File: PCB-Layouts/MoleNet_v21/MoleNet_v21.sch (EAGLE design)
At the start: 31 parts, among them IC1 25LC080P, Q1 BS250, Q2 BS170, U1 MCP1703-5002E/DB, U2 ATMEGA328P-PU, U3 RFM69CW, X1 SMA-142-0711-821/826

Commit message: MoleNet version 2.1 ready
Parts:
- added JP7: (no value), pinhead:PINHD-1X6
- added JP8: (no value), pinhead:PINHD-1X3
- JP3: value ISP -> (none); device pinhead:PINHD-2X5 -> pinhead:PINHD-1X3
- JP4: device pinhead:PINHD-1X4 -> pinhead:PINHD-1X3
- JP6: value (none) -> ISP; device pinhead:PINHD-1X6 -> pinhead:PINHD-2X5
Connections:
- new net N$2: JP3.2, Q1.S, R2.2
- new net SENSRXD: C11.1, JP8.3, K1.3
- net +12V: now also JP3.1; no longer Q1.S, R2.2
- net D4: now also JP4.3; no longer JP4.4
- net D5: now also JP4.2; no longer JP4.3
- net D6: now also JP4.1; no longer JP4.2
- net D8: now also JP8.1; no longer JP4.1
- net GND: now also JP6.10, JP6.4, JP6.8, JP7.5, JP7.6; no longer JP3.10, JP3.4, JP3.6, JP3.8, JP6.5
- net MISO: now also JP6.9; no longer JP3.9
- net MOSI: now also JP6.1; no longer JP3.1
- net N$9: now also JP7.1; no longer JP6.1
- net RESET: now also JP6.5; no longer JP3.5
- net RXD: now also JP7.3, JP8.2; no longer C11.1, JP6.3, K1.3
- net SCK: now also JP6.7; no longer JP3.7
- net TXD: now also JP7.2; no longer JP6.2
- net VCC: now also JP3.3, JP6.2, JP7.4; no longer JP3.2, JP6.4
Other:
- moved on the sheet: C11, C12, K1, Q1, Q2, R2, RTC-1, RTC-2, RTC-3, RTC-4, RTC-5, RTC-6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

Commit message: MoleNet version 2.1 rtm
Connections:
- net RXD: now also JP8.3; no longer JP8.2
- net SENSRXD: now also JP8.2; no longer JP8.3
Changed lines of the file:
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@@
-</segment>
-<segment>
-<wire x1="210.82" y1="38.1" x2="195.58" y2="38.1" width="0.1524" layer="91"/>
-<label x="195.58" y="38.1" size="1.778" layer="95"/>
-<pinref part="JP8" gate="A" pin="2"/>
 </segment>
 <segment>
@@
 <wire x1="50.8" y1="40.64" x2="35.56" y2="40.64" width="0.1524" layer="91"/>
 <label x="35.56" y="40.64" size="1.778" layer="95"/>
+</segment>
+<segment>
+<wire x1="210.82" y1="35.56" x2="195.58" y2="35.56" width="0.1524" layer="91"/>
+<label x="195.58" y="35.56" size="1.778" layer="95"/>
+<pinref part="JP8" gate="A" pin="3"/>
 </segment>
 </net>
@@
 <net name="SENSRXD" class="0">
 <segment>
-<wire x1="210.82" y1="35.56" x2="195.58" y2="35.56" width="0.1524" layer="91"/>
-<label x="195.58" y="35.56" size="1.778" layer="95"/>
-<pinref part="JP8" gate="A" pin="3"/>
-</segment>
-<segment>
 <pinref part="K1" gate="G$1" pin="3"/>
 <label x="154.94" y="30.48" size="1.778" layer="95"/>
 <pinref part="C11" gate="G$1" pin="1"/>
 <wire x1="165.1" y1="30.48" x2="152.4" y2="30.48" width="0.1524" layer="91"/>
+</segment>
+<segment>
+<wire x1="210.82" y1="38.1" x2="195.58" y2="38.1" width="0.1524" layer="91"/>
+<label x="195.58" y="38.1" size="1.778" layer="95"/>
+<pinref part="JP8" gate="A" pin="2"/>
 </segment>
 </net>
@@
 </sheet>
 </sheets>
-<errors>
-</errors>
 </schematic>
 </drawing>

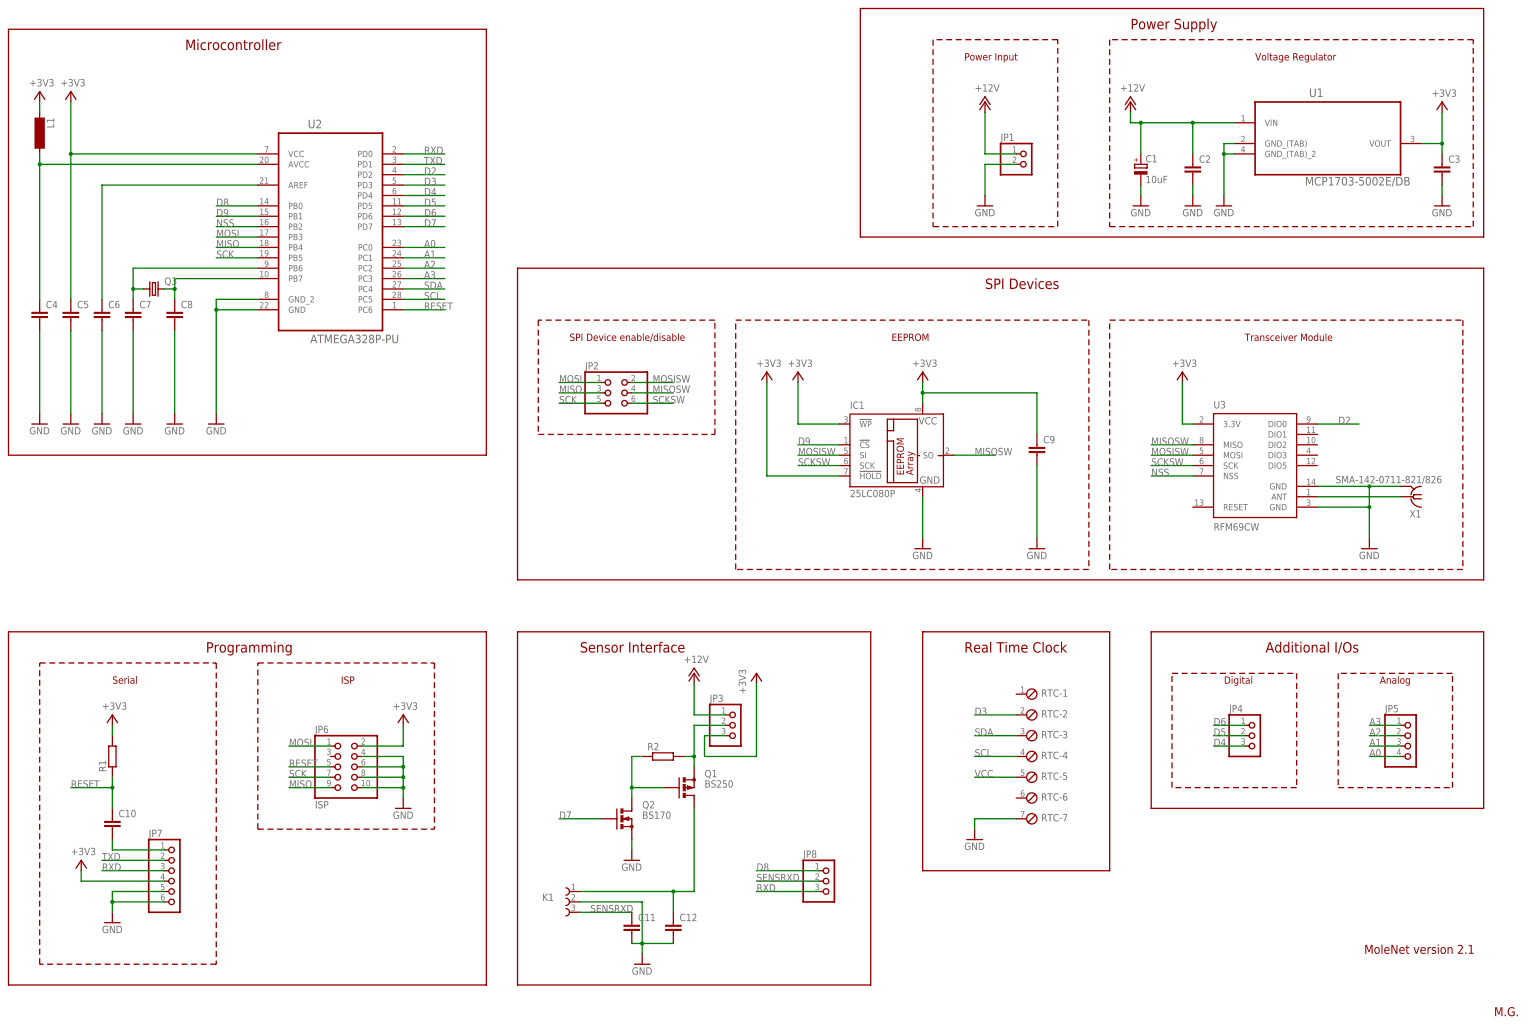
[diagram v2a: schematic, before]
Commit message: added/corrected part values in all layouts; created partlist for version 2.1
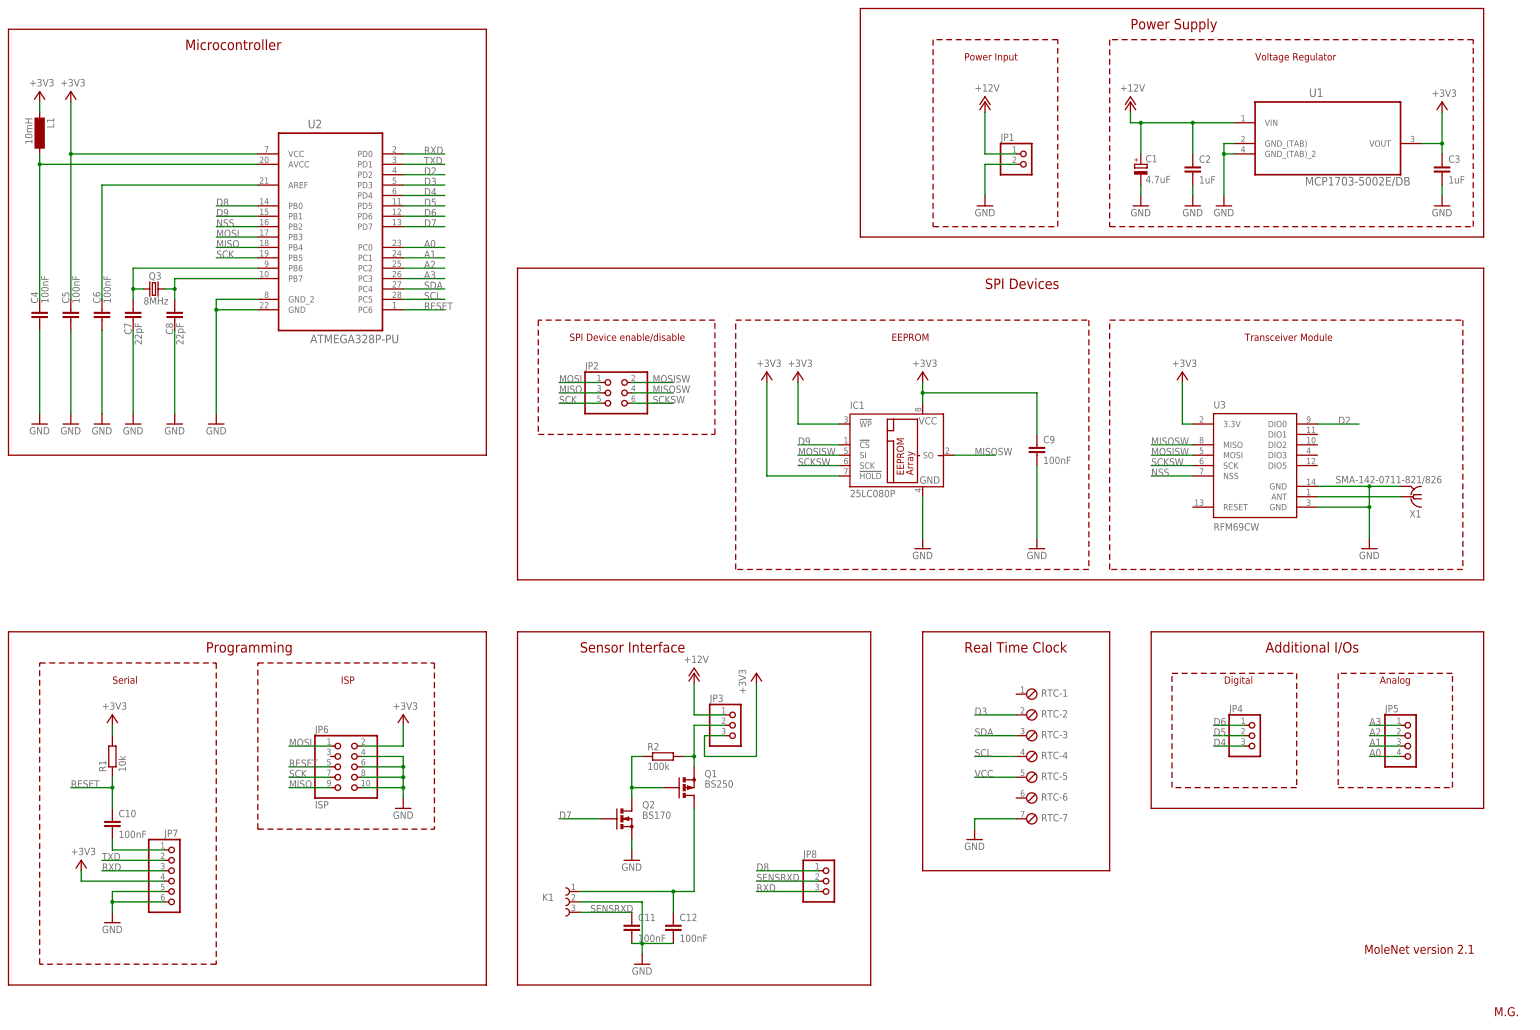
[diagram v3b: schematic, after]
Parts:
- C1: value 10uF -> 4.7uF
- C10, C11, C12, C4, C5, C6, C9: value (none) -> 100nF
- C2, C3: value (none) -> 1uF
- C7, C8: value (none) -> 22pF
- L1: value (none) -> 10mH
- Q3: value (none) -> 8MHz
- R1: value (none) -> 10k
- R2: value (none) -> 100k
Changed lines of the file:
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@@
 <setting verticaltext="up"/>
 </settings>
-<grid distance="0.1" unitdist="inch" unit="inch" style="lines" multiple="1" display="yes" altdistance="0.01" altunitdist="inch" altunit="inch"/>
+<grid distance="100" unitdist="mil" unit="mil" style="lines" multiple="1" display="no" altdistance="0.01" altunitdist="inch" altunit="inch"/>
 <layers>
 <layer number="1" name="Top" color="4" fill="1" visible="no" active="no"/>
@@
 <part name="Q1" library="transistor-small-signal" deviceset="BS250" device=""/>
 <part name="GND1" library="supply1" deviceset="GND" device=""/>
-<part name="R2" library="resistor" deviceset="R-EU_" device="0207/10"/>
+<part name="R2" library="resistor" deviceset="R-EU_" device="0207/10" value="100k"/>
 <part name="+3V1" library="supply1" deviceset="+3V3" device=""/>
 <part name="GND2" library="supply1" deviceset="GND" device=""/>
-<part name="L1" library="inductor-neosid" deviceset="BS" device="11"/>
-<part name="C1" library="resistor" deviceset="CPOL-EU" device="E2.5-6" value="10uF"/>
-<part name="C2" library="resistor" deviceset="C-EU" device="025-025X050"/>
-<part name="C3" library="resistor" deviceset="C-EU" device="025-025X050"/>
-<part name="C4" library="resistor" deviceset="C-EU" device="025-025X050"/>
+<part name="L1" library="inductor-neosid" deviceset="BS" device="11" value="10mH"/>
+<part name="C1" library="resistor" deviceset="CPOL-EU" device="E2.5-6" value="4.7uF"/>
+<part name="C2" library="resistor" deviceset="C-EU" device="025-025X050" value="1uF"/>
+<part name="C3" library="resistor" deviceset="C-EU" device="025-025X050" value="1uF"/>
+<part name="C4" library="resistor" deviceset="C-EU" device="025-025X050" value="100nF"/>
 <part name="GND3" library="supply1" deviceset="GND" device=""/>
-<part name="C6" library="resistor" deviceset="C-EU" device="025-025X050"/>
+<part name="C6" library="resistor" deviceset="C-EU" device="025-025X050" value="100nF"/>
 <part name="GND4" library="supply1" deviceset="GND" device=""/>
 <part name="+3V2" library="supply1" deviceset="+3V3" device=""/>
@@
 <part name="GND12" library="supply1" deviceset="GND" device=""/>
 <part name="FRAME1" library="frames" deviceset="A3L-LOC" device=""/>
-<part name="C5" library="resistor" deviceset="C-EU" device="025-025X050"/>
+<part name="C5" library="resistor" deviceset="C-EU" device="025-025X050" value="100nF"/>
 <part name="GND13" library="supply1" deviceset="GND" device=""/>
 <part name="JP7" library="pinhead" deviceset="PINHD-1X6" device=""/>
 <part name="GND14" library="supply1" deviceset="GND" device=""/>
 <part name="+3V8" library="supply1" deviceset="+3V3" device=""/>
-<part name="C10" library="resistor" deviceset="C-EU" device="025-025X050"/>
-<part name="R1" library="resistor" deviceset="R-EU_" device="0207/10"/>
+<part name="C10" library="resistor" deviceset="C-EU" device="025-025X050" value="100nF"/>
+<part name="R1" library="resistor" deviceset="R-EU_" device="0207/10" value="10k"/>
 <part name="+3V9" library="supply1" deviceset="+3V3" device=""/>
-<part name="Q3" library="crystal" deviceset="CRYSTAL" device="HC18U-V"/>
-<part name="C7" library="resistor" deviceset="C-EU" device="025-025X050"/>
-<part name="C8" library="resistor" deviceset="C-EU" device="025-025X050"/>
+<part name="Q3" library="crystal" deviceset="CRYSTAL" device="HC18U-V" value="8MHz"/>
+<part name="C7" library="resistor" deviceset="C-EU" device="025-025X050" value="22pF"/>
+<part name="C8" library="resistor" deviceset="C-EU" device="025-025X050" value="22pF"/>
 <part name="GND16" library="supply1" deviceset="GND" device=""/>
 <part name="GND17" library="supply1" deviceset="GND" device=""/>
@@
 <part name="GND18" library="supply1" deviceset="GND" device=""/>
 <part name="+3V10" library="supply1" deviceset="+3V3" device=""/>
-<part name="C9" library="resistor" deviceset="C-EU" device="025-025X050"/>
+<part name="C9" library="resistor" deviceset="C-EU" device="025-025X050" value="100nF"/>
 <part name="GND19" library="supply1" deviceset="GND" device=""/>
-<part name="C11" library="resistor" deviceset="C-EU" device="025-025X050"/>
-<part name="C12" library="resistor" deviceset="C-EU" device="025-025X050"/>
+<part name="C11" library="resistor" deviceset="C-EU" device="025-025X050" value="100nF"/>
+<part name="C12" library="resistor" deviceset="C-EU" device="025-025X050" value="100nF"/>
 <part name="JP2" library="pinhead" deviceset="PINHD-2X3" device=""/>
 <part name="JP5" library="pinhead" deviceset="PINHD-1X4" device=""/>
@@
 <instance part="C2" gate="G$1" x="302.26" y="213.36"/>
 <instance part="C3" gate="G$1" x="363.22" y="213.36"/>
-<instance part="C4" gate="G$1" x="20.32" y="177.8"/>
+<instance part="C4" gate="G$1" x="20.32" y="177.8" smashed="yes">
+<attribute name="NAME" x="19.939" y="179.324" size="1.778" layer="95" rot="R90"/>
+<attribute name="VALUE" x="22.479" y="179.324" size="1.778" layer="96" rot="R90"/>
+</instance>
 <instance part="GND3" gate="1" x="20.32" y="149.86"/>
-<instance part="C6" gate="G$1" x="35.56" y="177.8"/>
+<instance part="C6" gate="G$1" x="35.56" y="177.8" smashed="yes">
+<attribute name="NAME" x="35.179" y="179.324" size="1.778" layer="95" rot="R90"/>
+<attribute name="VALUE" x="37.719" y="179.324" size="1.778" layer="96" rot="R90"/>
+</instance>
 <instance part="GND4" gate="1" x="35.56" y="149.86"/>
 <instance part="+3V2" gate="G$1" x="27.94" y="231.14" smashed="yes">
@@
 <instance part="GND12" gate="1" x="309.88" y="203.2"/>
 <instance part="FRAME1" gate="G$1" x="0" y="0"/>
-<instance part="C5" gate="G$1" x="27.94" y="177.8"/>
+<instance part="C5" gate="G$1" x="27.94" y="177.8" smashed="yes">
+<attribute name="NAME" x="27.559" y="179.324" size="1.778" layer="95" rot="R90"/>
+<attribute name="VALUE" x="30.099" y="179.324" size="1.778" layer="96" rot="R90"/>
+</instance>
 <instance part="GND13" gate="1" x="27.94" y="149.86"/>
-<instance part="JP7" gate="A" x="53.34" y="38.1"/>
+<instance part="JP7" gate="A" x="53.34" y="38.1" smashed="yes">
+<attribute name="NAME" x="50.8" y="48.895" size="1.778" layer="95"/>
+<attribute name="VALUE" x="46.99" y="27.94" size="1.778" layer="96"/>
+</instance>
 <instance part="GND14" gate="1" x="38.1" y="27.94"/>
 <instance part="+3V8" gate="G$1" x="30.48" y="43.18" smashed="yes">
@@
 <attribute name="VALUE" x="35.56" y="80.01" size="1.778" layer="96"/>
 </instance>
-<instance part="Q3" gate="G$1" x="48.26" y="182.88"/>
-<instance part="C7" gate="G$1" x="43.18" y="177.8"/>
-<instance part="C8" gate="G$1" x="53.34" y="177.8"/>
+<instance part="Q3" gate="G$1" x="48.26" y="182.88" smashed="yes">
+<attribute name="NAME" x="46.99" y="185.166" size="1.778" layer="95"/>
+<attribute name="VALUE" x="45.72" y="179.07" size="1.778" layer="96"/>
+</instance>
+<instance part="C7" gate="G$1" x="43.18" y="177.8" smashed="yes">
+<attribute name="NAME" x="42.799" y="171.704" size="1.778" layer="95" rot="R90"/>
+<attribute name="VALUE" x="45.339" y="169.164" size="1.778" layer="96" rot="R90"/>
+</instance>
+<instance part="C8" gate="G$1" x="53.34" y="177.8" smashed="yes">
+<attribute name="NAME" x="52.959" y="171.704" size="1.778" layer="95" rot="R90"/>
+<attribute name="VALUE" x="55.499" y="169.164" size="1.778" layer="96" rot="R90"/>
+</instance>
 <instance part="GND16" gate="1" x="43.18" y="149.86"/>
 <instance part="GND17" gate="1" x="53.34" y="149.86"/>
